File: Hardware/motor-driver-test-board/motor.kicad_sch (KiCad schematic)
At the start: 8 parts, among them J1 Conn_01x14, J2 Conn_01x08

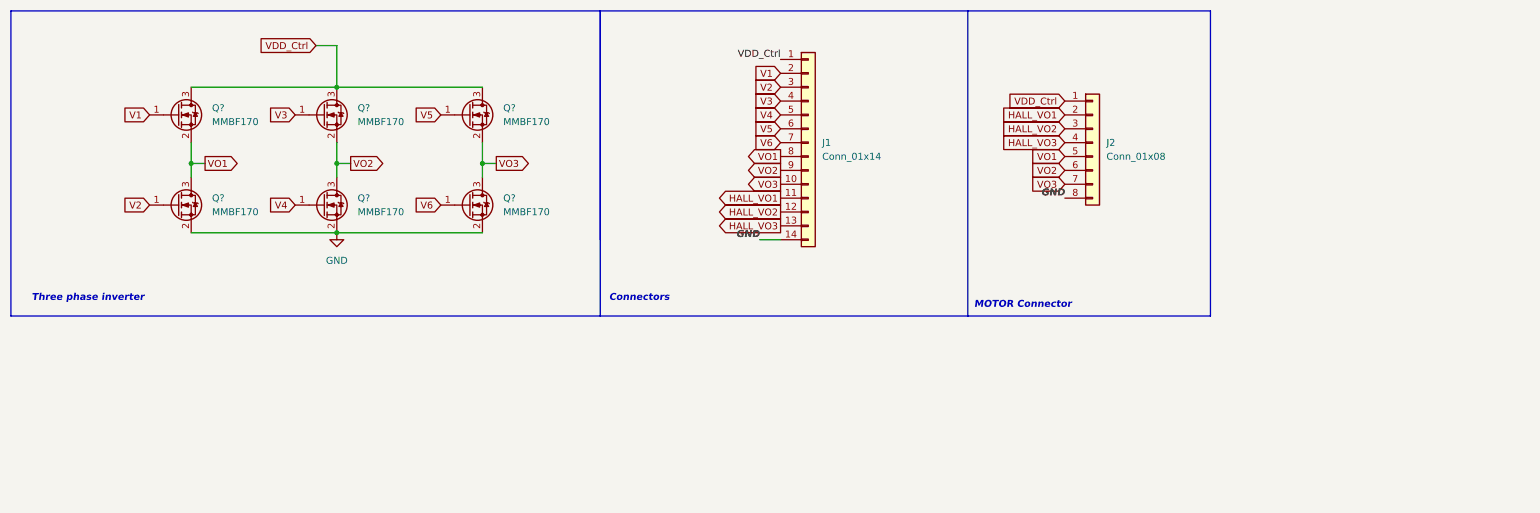
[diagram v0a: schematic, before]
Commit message: layout initialised and redundant u v w signals taken away from J1
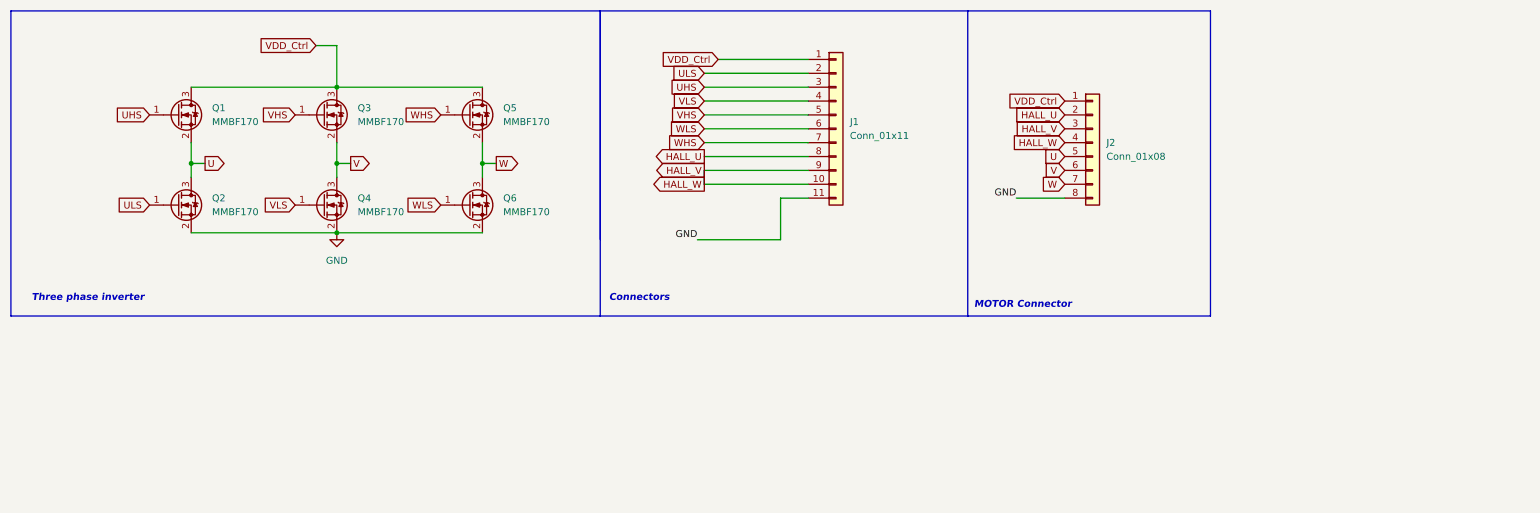
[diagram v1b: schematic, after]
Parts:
- removed J1: Conn_01x14, Connector_PinHeader_2.54mm:PinHeader_1x14_P2.54mm_Horizontal, symbol Connector_Generic:Conn_01x14
- added J1: Conn_01x11, symbol Connector_Generic:Conn_01x11
- J2: footprint Connector_PinHeader_1.00mm:PinHeader_1x08_P1.00mm_Vertical -> Connector_PinHeader_1.00mm:PinHeader_1x08_P1.00mm_Horizontal
- gave numbers to parts that had none: 6
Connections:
- net HALL_VO3 is gone; now on net HALL_V: J2.4 (Pin_4)
- net GND: now also J1.11 (Pin_11)
- net VDD_Ctrl: now also J1.1 (Pin_1)
- net HALL_VO1 renamed HALL_U
- net HALL_U: now also J1.8 (Pin_8)
- net HALL_VO2 renamed HALL_V
- net HALL_V: now also J1.10 (Pin_10), J1.9 (Pin_9)
- net V1 renamed UHS
- net UHS: now also J1.3 (Pin_3)
- net V2 renamed ULS
- net ULS: now also J1.2 (Pin_2)
- net V3 renamed VHS
- net VHS: now also J1.5 (Pin_5)
- net V4 renamed VLS
- net VLS: now also J1.4 (Pin_4)
- net V5 renamed WHS
- net WHS: now also J1.7 (Pin_7)
- net V6 renamed WLS
- net WLS: now also J1.6 (Pin_6)
- net VO1 renamed U
- net VO2 renamed V
- net VO3 renamed W

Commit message: PCB REV 1.0
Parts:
- J1: footprint (none) -> Connector_PinHeader_2.54mm:PinHeader_1x11_P2.54mm_Vertical
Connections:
- net GND: now also J2.1 (Pin_1); no longer J2.8 (Pin_8)
- net U: now also J2.4 (Pin_4); no longer J2.5 (Pin_5)
- net UHS: now also J1.8 (Pin_8); no longer J1.3 (Pin_3)
- net ULS: now also J1.5 (Pin_5); no longer J1.2 (Pin_2)
- net V: now also J2.3 (Pin_3); no longer J2.6 (Pin_6)
- net VDD_Ctrl: now also J2.8 (Pin_8); no longer J2.1 (Pin_1)
- net VHS: now also J1.9 (Pin_9); no longer J1.5 (Pin_5)
- net VLS: now also J1.6 (Pin_6); no longer J1.4 (Pin_4)
- net W: now also J2.2 (Pin_2); no longer J2.7 (Pin_7)
- net WHS: now also J1.10 (Pin_10); no longer J1.7 (Pin_7)
- net WLS: now also J1.7 (Pin_7); no longer J1.6 (Pin_6)
- removed net HALL_U: J1.8 (Pin_8), J2.2 (Pin_2)
- removed net HALL_V: J1.10 (Pin_10), J1.9 (Pin_9), J2.3 (Pin_3), J2.4 (Pin_4)
- new net HU: J1.2 (Pin_2), J2.7 (Pin_7)
- new net HV: J1.3 (Pin_3), J2.6 (Pin_6)
- new net HW: J1.4 (Pin_4), J2.5 (Pin_5)

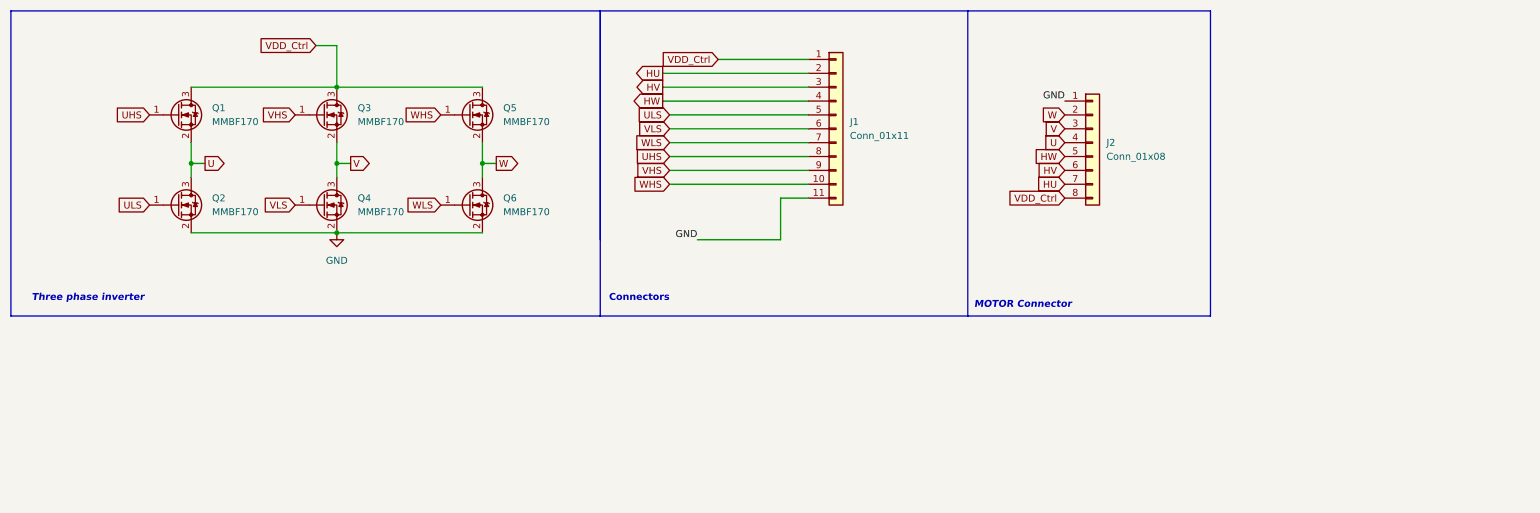
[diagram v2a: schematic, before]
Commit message: power polygons changed to trace, connector position shifted to the edge and boundary changed
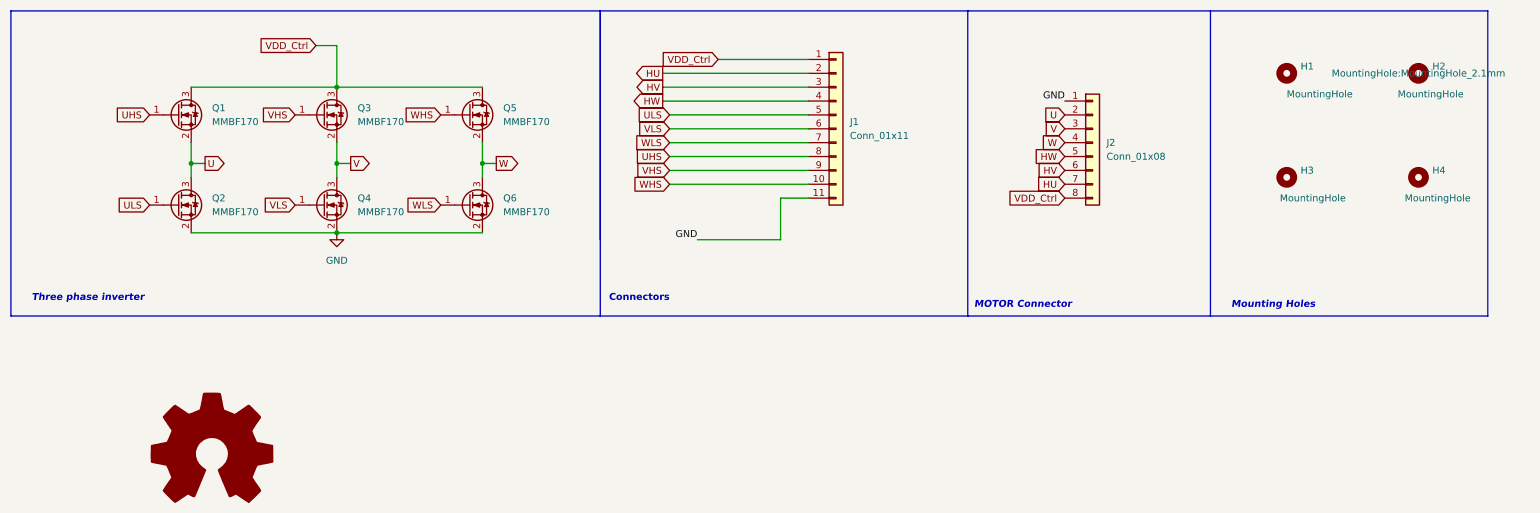
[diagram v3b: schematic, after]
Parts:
- added H1, H2, H3, H4: MountingHole, MountingHole:MountingHole_2.1mm, symbol Mechanical:MountingHole
- J1: footprint Connector_PinHeader_2.54mm:PinHeader_1x11_P2.54mm_Vertical -> Connector_PinHeader_2.54mm:PinHeader_1x11_P2.54mm_Horizontal
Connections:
- net U: now also J2.2 (Pin_2); no longer J2.4 (Pin_4)
- net W: now also J2.4 (Pin_4); no longer J2.2 (Pin_2)
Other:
- note added: "Mounting Holes"
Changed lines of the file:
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@@
+    (stroke (width 0) (type default) (color 0 0 0 0))
+  )
+  (polyline (pts (xy 283.21 68.58) (xy 232.41 68.58))
     (stroke (width 0) (type default) (color 0 0 0 0))
   )
@@
     (stroke (width 0) (type default) (color 0 0 0 0))
   )
+  (polyline (pts (xy 232.41 12.7) (xy 283.21 12.7))
+    (stroke (width 0) (type default) (color 0 0 0 0))
+  )
   (wire (pts (xy 99.06 40.64) (xy 99.06 43.18))
     (stroke (width 0) (type default) (color 0 0 0 0))
@@
   )
   (wire (pts (xy 72.39 36.83) (xy 72.39 40.64))
+    (stroke (width 0) (type default) (color 0 0 0 0))
+  )
+  (polyline (pts (xy 283.21 12.7) (xy 283.21 68.58))
     (stroke (width 0) (type default) (color 0 0 0 0))
   )
@@
     (effects (font (size 1.27 1.27) bold italic) (justify right bottom))
   )
+  (text "Mounting Holes" (at 236.22 67.31 0)
+    (effects (font (size 1.27 1.27) (thickness 0.254) bold italic) (justify left bottom))
+  )
   (text "Connectors" (at 133.35 66.04 180)
     (effects (font (size 1.27 1.27) (thickness 0.254) bold) (justify right bottom))
@@
   (global_label "V" (shape input) (at 205.74 34.29 180) (fields_autoplaced)
     (effects (font (size 1.27 1.27)) (justify right))
-    (property "Intersheet References" "${INTERSHEET_REFS}" (id 0) (at 202.2383 34.3694 0)
+    (property "Intersheet References" "${INTERSHEET_REFS}" (id 0) (at 202.2383 34.2106 0)
       (effects (font (size 1.27 1.27)) (justify right) hide)
     )
@@
     )
   )
-  (global_label "U" (shape input) (at 205.74 36.83 180) (fields_autoplaced)
-    (effects (font (size 1.27 1.27)) (justify right))
-    (property "Intersheet References" "${INTERSHEET_REFS}" (id 0) (at 201.9964 36.9094 0)
+  (global_label "U" (shape input) (at 205.74 31.75 180) (fields_autoplaced)
+    (effects (font (size 1.27 1.27)) (justify right))
+    (property "Intersheet References" "${INTERSHEET_REFS}" (id 0) (at 201.9964 31.6706 0)
       (effects (font (size 1.27 1.27)) (justify right) hide)
     )
@@
     )
   )
-  (global_label "W" (shape input) (at 205.74 31.75 180) (fields_autoplaced)
-    (effects (font (size 1.27 1.27)) (justify right))
-    (property "Intersheet References" "${INTERSHEET_REFS}" (id 0) (at 201.8755 31.8294 0)
+  (global_label "W" (shape input) (at 205.74 36.83 180) (fields_autoplaced)
+    (effects (font (size 1.27 1.27)) (justify right))
+    (property "Intersheet References" "${INTERSHEET_REFS}" (id 0) (at 201.8755 36.7506 0)
       (effects (font (size 1.27 1.27)) (justify right) hide)
     )
@@
     (pin "3")
   )
+  (symbol (lib_id "Mechanical:MountingHole") (at 270.51 43.18 0) (unit 1)
+    (in_bom yes) (on_board yes)
+    (property "Reference" "H4" (id 0) (at 273.05 41.9099 0)
+      (effects (font (size 1.27 1.27)) (justify left))
+    )
+    (property "Value" "MountingHole" (id 1) (at 267.97 46.99 0)
+      (effects (font (size 1.27 1.27)) (justify left))
+    )
+    (property "Footprint" "MountingHole:MountingHole_2.1mm" (id 2) (at 270.51 43.18 0)
+      (effects (font (size 1.27 1.27)) hide)
+    )
+    (property "Datasheet" "~" (id 3) (at 270.51 43.18 0)
+      (effects (font (size 1.27 1.27)) hide)
+    )
+  )
   (symbol (lib_id "Transistor_FET:MMBF170") (at 69.85 48.26 0) (unit 1)
     (in_bom yes) (on_board yes) (fields_autoplaced)
@@
     (pin "3")
   )
+  (symbol (lib_id "Mechanical:MountingHole") (at 270.51 24.13 0) (unit 1)
+    (in_bom yes) (on_board yes)
+    (property "Reference" "H2" (id 0) (at 273.05 22.8599 0)
+      (effects (font (size 1.27 1.27)) (justify left))
+    )
+    (property "Value" "MountingHole" (id 1) (at 266.7 27.94 0)
+      (effects (font (size 1.27 1.27)) (justify left))
+    )
+    (property "Footprint" "MountingHole:MountingHole_2.1mm" (id 2) (at 270.51 24.13 0))
+    (property "Datasheet" "~" (id 3) (at 270.51 24.13 0)
+      (effects (font (size 1.27 1.27)) hide)
+    )
+  )
   (symbol (lib_id "Connector_Generic:Conn_01x11") (at 163.83 34.29 0) (unit 1)
     (in_bom yes) (on_board yes) (fields_autoplaced)
@@
       (effects (font (size 1.27 1.27)) (justify left))
     )
-    (property "Footprint" "Connector_PinHeader_2.54mm:PinHeader_1x11_P2.54mm_Vertical" (id 2) (at 163.83 34.29 0)
+    (property "Footprint" "Connector_PinHeader_2.54mm:PinHeader_1x11_P2.54mm_Horizontal" (id 2) (at 163.83 34.29 0)
       (effects (font (size 1.27 1.27)) hide)
     )
@@
     (pin "3")
   )
+  (symbol (lib_id "Mechanical:MountingHole") (at 246.38 24.13 0) (unit 1)
+    (in_bom yes) (on_board yes)
+    (property "Reference" "H1" (id 0) (at 248.92 22.8599 0)
+      (effects (font (size 1.27 1.27)) (justify left))
+    )
+    (property "Value" "MountingHole" (id 1) (at 246.38 27.94 0)
+      (effects (font (size 1.27 1.27)) (justify left))
+    )
+    (property "Footprint" "MountingHole:MountingHole_2.1mm" (id 2) (at 246.38 24.13 0)
+      (effects (font (size 1.27 1.27)) hide)
+    )
+    (property "Datasheet" "~" (id 3) (at 246.38 24.13 0)
+      (effects (font (size 1.27 1.27)) hide)
+    )
+  )
+  (symbol (lib_id "Graphic:Logo_Open_Hardware_Large") (at 49.53 93.98 0) (unit 1)
+    (in_bom yes) (on_board yes) (fields_autoplaced)
+    (property "Reference" "#LOGO1" (id 0) (at 49.53 81.28 0)
+      (effects (font (size 1.27 1.27)) hide)
+    )
+    (property "Value" "Logo_Open_Hardware_Large" (id 1) (at 49.53 104.14 0)
+      (effects (font (size 1.27 1.27)) hide)
+    )
+    (property "Footprint" "motor-driver-test-board:better_logo" (id 2) (at 49.53 93.98 0)
+      (effects (font (size 1.27 1.27)) hide)
+    )
+    (property "Datasheet" "~" (id 3) (at 49.53 93.98 0)
+      (effects (font (size 1.27 1.27)) hide)
+    )
+  )
   (symbol (lib_id "Connector_Generic:Conn_01x08") (at 210.82 36.83 0) (unit 1)
     (in_bom yes) (on_board yes) (fields_autoplaced)
@@
     (pin "3")
   )
+  (symbol (lib_id "Mechanical:MountingHole") (at 246.38 43.18 0) (unit 1)
+    (in_bom yes) (on_board yes)
+    (property "Reference" "H3" (id 0) (at 248.92 41.9099 0)
+      (effects (font (size 1.27 1.27)) (justify left))
+    )
+    (property "Value" "MountingHole" (id 1) (at 245.11 46.99 0)
+      (effects (font (size 1.27 1.27)) (justify left))
+    )
+    (property "Footprint" "MountingHole:MountingHole_2.1mm" (id 2) (at 246.38 43.18 0)
+      (effects (font (size 1.27 1.27)) hide)
+    )
+    (property "Datasheet" "~" (id 3) (at 246.38 43.18 0)
+      (effects (font (size 1.27 1.27)) hide)
+    )
+  )
   (symbol (lib_id "power:GND") (at 72.39 53.34 0) (unit 1)
     (in_bom yes) (on_board yes) (fields_autoplaced)
@@
   )
   (symbol_instances
+    (path "/a55ae76b-9b49-46b2-bf8c-ffe197b9079e"
+      (reference "#LOGO1") (unit 1) (value "Logo_Open_Hardware_Large") (footprint "motor-driver-test-board:better_logo")
+    )
     (path "/ebe441ed-8290-4f69-9565-ac043222b83d"
       (reference "#PWR0101") (unit 1) (value "GND") (footprint "")
     )
+    (path "/a1817e88-7c7d-4928-9354-21f63424d118"
+      (reference "H1") (unit 1) (value "MountingHole") (footprint "MountingHole:MountingHole_2.1mm")
+    )
+    (path "/397f77e9-c24c-4060-883f-c5d27d69d23b"
+      (reference "H2") (unit 1) (value "MountingHole") (footprint "MountingHole:MountingHole_2.1mm")
+    )
+    (path "/d06612c9-858f-4c3d-95a4-dcb499a72894"
+      (reference "H3") (unit 1) (value "MountingHole") (footprint "MountingHole:MountingHole_2.1mm")
+    )
+    (path "/331eb311-64b4-4082-b47a-0a9de43efe10"
+      (reference "H4") (unit 1) (value "MountingHole") (footprint "MountingHole:MountingHole_2.1mm")
+    )
     (path "/5bb63f7a-1567-497e-84a4-f6f3c10f55de"
-      (reference "J1") (unit 1) (value "Conn_01x11") (footprint "Connector_PinHeader_2.54mm:PinHeader_1x11_P2.54mm_Vertical")
+      (reference "J1") (unit 1) (value "Conn_01x11") (footprint "Connector_PinHeader_2.54mm:PinHeader_1x11_P2.54mm_Horizontal")
     )
     (path "/ba3d1fd9-cdeb-4bfa-9fda-d99a3e9e268d"
